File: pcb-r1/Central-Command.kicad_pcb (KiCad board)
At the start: 4 copper layers, 38.1 x 63.5 mm, 60 parts, among them P101 CONN_01X10, P102 CONN_01X10, P103 CONN_01X04, P104 CONN_01X02, P105 CONN_01X04, P106 CONN_01X02, P201 CONN_01X06, P202 CONN_01X04, P203 CONN_01X04, P204 CONN_01X03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

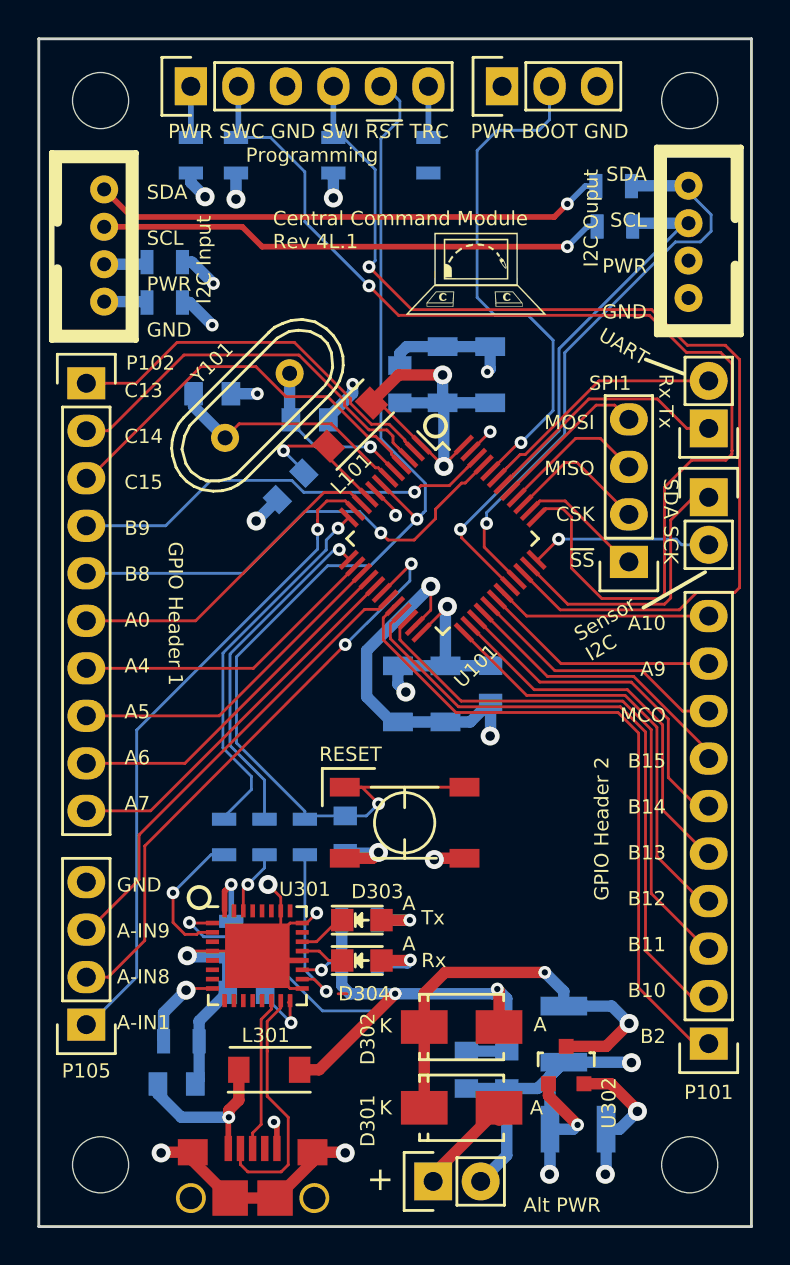
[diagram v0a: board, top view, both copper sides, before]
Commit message: Completed revised board 4L.2 and submitted to OSH Park
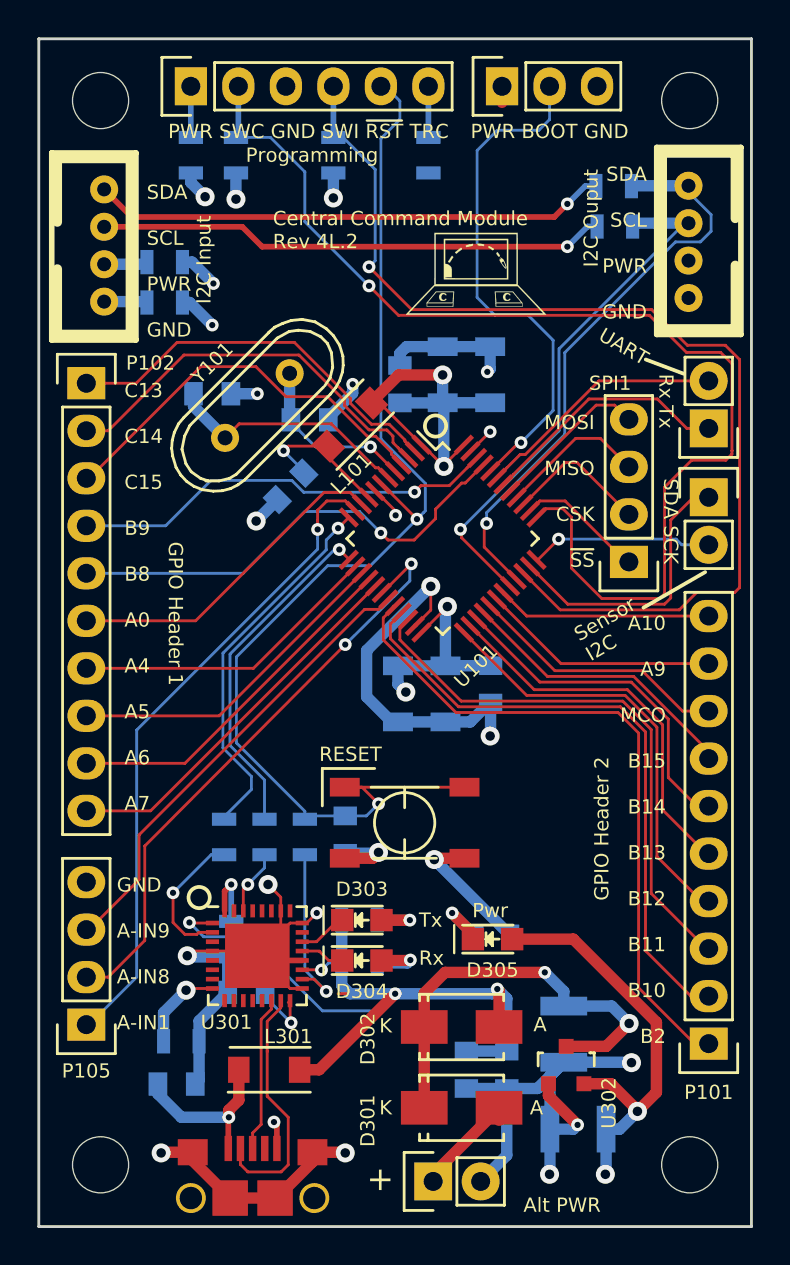
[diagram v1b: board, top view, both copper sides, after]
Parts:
- added D305: Pwr LED, CentralCommand:LED-0805, F.Cu at (100.5, 124.3)
- added R308: 270Ω, Resistors_SMD:R_0805, B.Cu at (100.6, 124.2)
- D303, D304: footprint LEDs:LED-0805 -> CentralCommand:LED-0805
- moved G*** 21.6 mm to (84.3, 109.2), turned to 270 degrees
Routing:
- net /Comm/PWR: track 46.4 -> 62.0 mm
- net GND: track 112.9 -> 118.8 mm
- net Net-(D305-Pad1): track 0.00 -> 3.72 mm, vias 0 -> 1
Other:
- board text added: "Central Command Module Rev 4L.2"
- board text added: "Pwr"
- board text removed: "A"
- board text removed: "Central Command Module Rev 4L.1"
